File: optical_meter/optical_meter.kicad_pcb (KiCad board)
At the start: 4 copper layers, 100 x 100 mm, 47 parts, among them J1 Conn_02x04, J2 SFP+, J3 Conn_01x02_Pin, U2 LVDS -> LVTTL, U3 LVTTL -> LVDS, U5 Pico

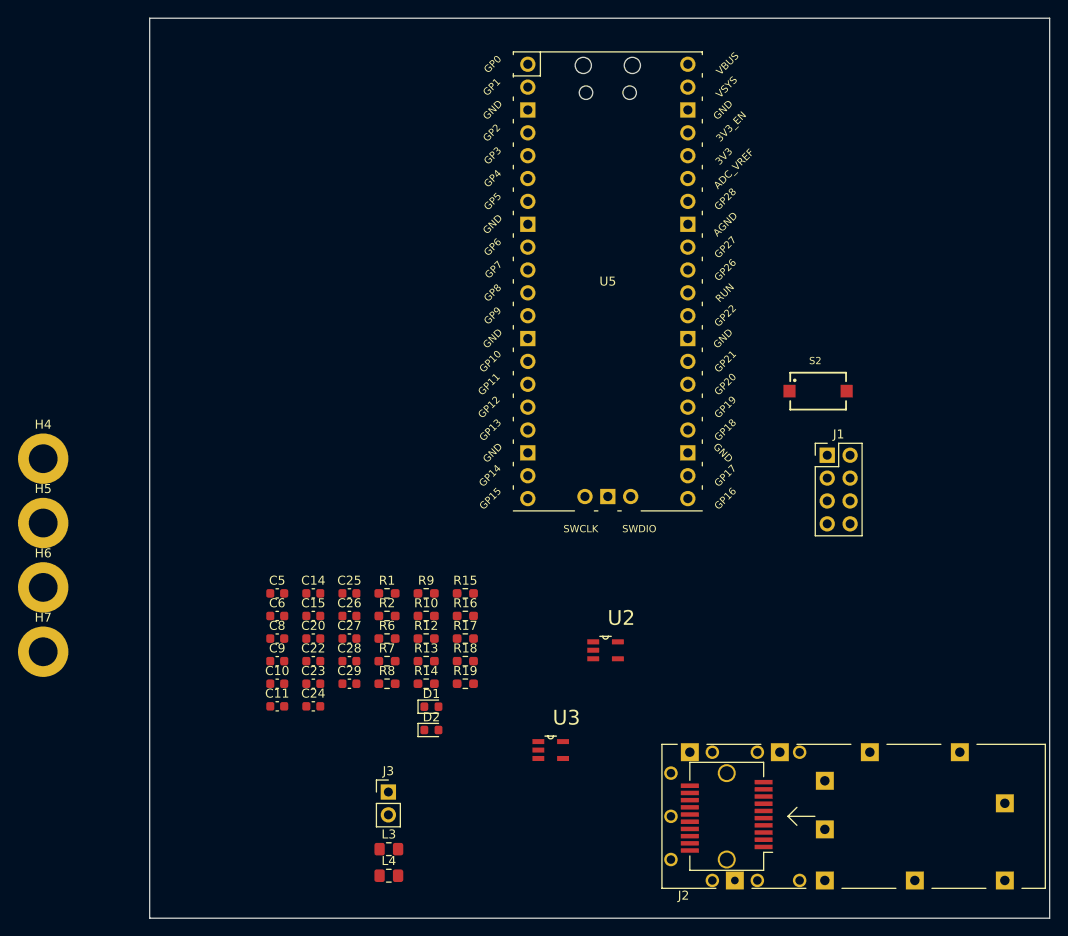
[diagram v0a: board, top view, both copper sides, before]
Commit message: Finished layout. DRC passed except for courtyard and some footprint-schematic relaitions from KiCad that do not matter
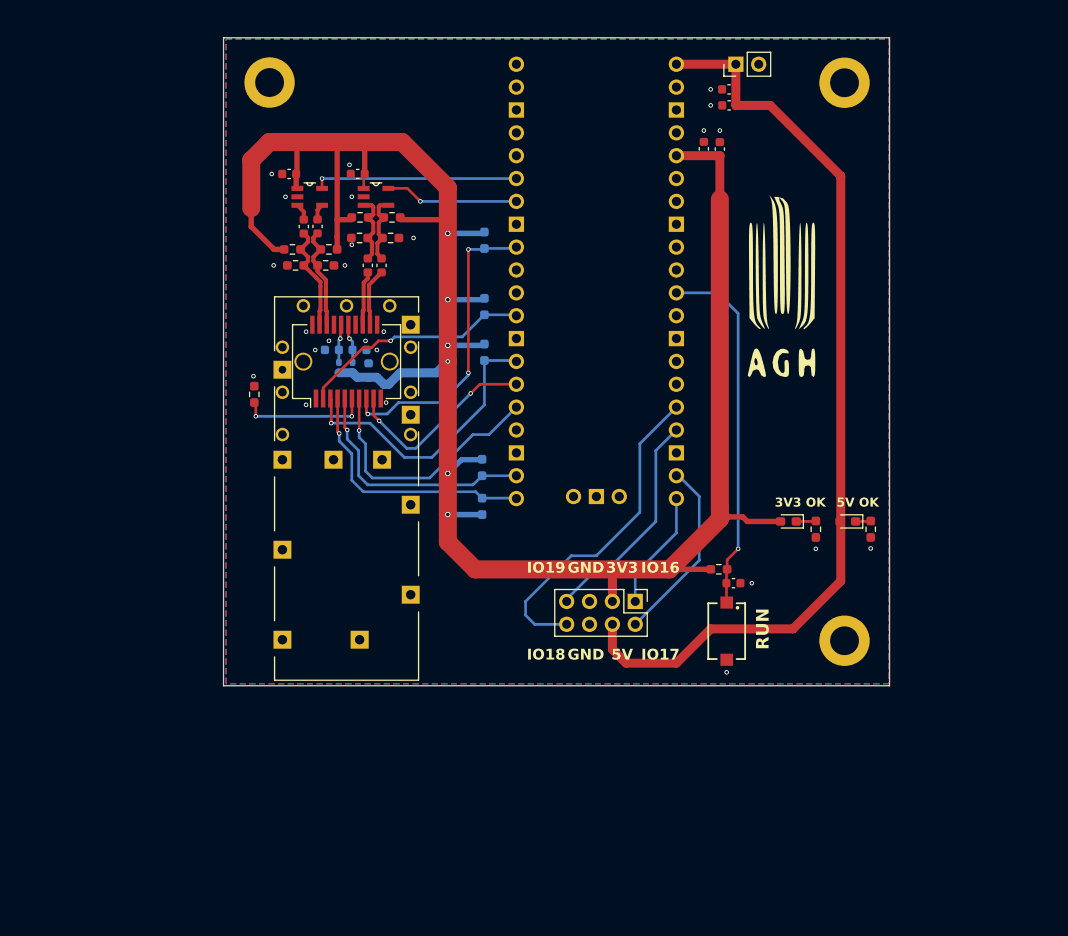
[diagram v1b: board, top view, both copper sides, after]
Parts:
- removed C11, C24, C5: 100n, Capacitor_SMD:C_0603_1608Metric
- removed C20: 2u2, Capacitor_SMD:C_0603_1608Metric
- removed H7: ~, MountingHole:MountingHole_3.2mm_M3_DIN965_Pad
- removed L3, L4: 1u, Inductor_SMD:L_0805_2012Metric_Pad1.15x1.40mm_HandSolder
- added C16: 2u2, Capacitor_SMD:C_0603_1608Metric, F.Cu at (229.9, 27.7)
- added FR1: BLM15HG102SN1D, Inductor_SMD:L_0402_1005Metric_Pad0.77x0.64mm_HandSolder, B.Cu at (186.5, 56.8)
- added FR4: BLM15HG102SN1D, Inductor_SMD:L_0402_1005Metric_Pad0.77x0.64mm_HandSolder, B.Cu at (188.0, 56.8)
- added G***: LOGO, AGH_LOGO:agh_logo, F.Cu at (235.7, 46.3)
- added R11: 4k7, Resistor_SMD:R_0603_1608Metric_Pad0.98x0.95mm_HandSolder, B.Cu at (202.4, 72.2)
- added R20: 4k7, Resistor_SMD:R_0603_1608Metric_Pad0.98x0.95mm_HandSolder, B.Cu at (202.4, 67.9)
- C10, C6, C8, R6, R7, R8: moved to B.Cu
- D1, D2: footprint Diode_SMD:D_0603_1608Metric -> LED_SMD:LED_0603_1608Metric_Pad1.05x0.95mm_HandSolder
- U2: value LVDS -> LVTTL -> FIN1002M5X
- U3: value LVTTL -> LVDS -> FIN1001M5X
- moved H5 101.6 mm to (242.7, 25.2)
- moved H4 91.3 mm to (242.7, 87.2)
- moved J3 89.6 mm to (230.6, 23.1), turned to 90 degrees
- moved C15 74.5 mm to (229.9, 25.9), turned to 180 degrees
- moved C28 69.2 mm to (227.1, 32.5), turned to 90 degrees
- moved C27 68.2 mm to (228.9, 32.5), turned to 90 degrees
- moved J2 67.2 mm to (187.4, 50.0), turned to 90 degrees
- moved U3 67.0 mm to (183.3, 37.8)
- moved H6 61.5 mm to (178.8, 25.1)
- moved U2 56.5 mm to (190.7, 37.8)
- moved R1 54.2 mm to (245.6, 74.8), turned to -90 degrees
- moved C9 54.1 mm to (181.0, 35.3)
- moved R14 52.0 mm to (192.4, 40.1)
- moved C29 51.1 mm to (182.6, 41.1), turned to -90 degrees
- moved D1 50.6 mm to (243.1, 73.9), turned to 180 degrees
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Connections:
- J1 pad 1: /GPIO17 -> /GPIO16
- J1 pad 2: /GPIO16 -> /GPIO17
- J1 pad 7: /GPIO14 -> /GPIO18
- J1 pad 8: /GPIO15 -> /GPIO19
- R16 pad 1: /U3_TD+ -> /TD+
- R17 pad 2: /U3_TD+ -> /TD+
- R18 pad 1: /U3_TD- -> /TD-
- R19 pad 2: /U3_TD- -> /TD-
- U5 pad 10: /SCL -> unconnected-(U5-GPIO7-Pad10)
- U5 pad 11: /SDA -> unconnected-(U5-GPIO8-Pad11)
- U5 pad 14: /Rpi_TX -> /TX_DISABLE
- U5 pad 19: /GPIO14 -> /SCL
- U5 pad 20: /GPIO15 -> /SDA
- U5 pad 24: unconnected-(U5-GPIO18-Pad24) -> /GPIO18
- U5 pad 25: unconnected-(U5-GPIO19-Pad25) -> /GPIO19
- U5 pad 6: /Rpi_RX -> /Rpi_TX
- U5 pad 7: /TX_DISABLE -> /Rpi_RX
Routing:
- net +3V3: track 0.00 -> 233.3 mm, vias 0 -> 6
- net +5V: track 0.00 -> 103.7 mm
- net /RUN: track 0.00 -> 40.5 mm, vias 0 -> 1
- net /GPIO19: track 0.00 -> 37.4 mm
- net /RX_LOS: track 0.00 -> 34.2 mm, vias 0 -> 3
- net /TX_DISABLE: track 0.00 -> 32.3 mm, vias 0 -> 1
- net /SDA: track 0.00 -> 28.9 mm, vias 0 -> 1
- net /RS0: track 0.00 -> 28.7 mm, vias 0 -> 1
- net /SCL: track 0.00 -> 27.6 mm, vias 0 -> 1
- net /TX_FAULT: track 0.00 -> 26.3 mm, vias 0 -> 1
- net /GPIO18: track 0.00 -> 24.8 mm
- net /Rpi_TX: track 0.00 -> 22.7 mm, vias 0 -> 1
- net /RS1: track 0.00 -> 22.2 mm, vias 0 -> 2
- net /GPIO17: track 0.00 -> 20.7 mm
- net /Rpi_RX: track 0.00 -> 14.8 mm, vias 0 -> 1
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- added copper zone on B.Cu, net GND
- added copper zone on F.Cu, net GND
- added copper zone on In1.Cu, net GND
- added copper zone on In2.Cu, net GND
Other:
- board size 100 x 100 mm -> 74 x 72 mm
- board text added: "3V3"
- board text added: "3V3 OK"
- board text added: "5V"
- board text added: "5V OK"
- board text added: "GND"
- board text added: "IO16"
- board text added: "IO17"
- board text added: "IO18"
- board text added: "IO19"
- board text added: "PCB by Filip Kulka"
- board text added: "RUN"

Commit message: changing the layout (in progress)
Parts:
- removed G***: LOGO, AGH_LOGO:agh_logo
- removed the H4 at (242.7, 87.2)
- removed H5: ~, MountingHole:MountingHole_3.2mm_M3_DIN965_Pad
- removed the H6 at (178.8, 25.1)
- added H4: ~, MountingHole:MountingHole_3.2mm_M3_DIN965_Pad, F.Cu at (226.5, 85.3)
- added H4: ~, MountingHole:MountingHole_3.2mm_M3_DIN965_Pad, F.Cu at (174.5, 85.3)
- added H6: ~, MountingHole:MountingHole_3.2mm_M3_DIN965_Pad, F.Cu at (174.5, 26.3)
- added H6: ~, MountingHole:MountingHole_3.2mm_M3_DIN965_Pad, F.Cu at (226.5, 26.3)
- C10, C27: value 2u2 -> 4u7
- R11, R20, R6, R7, R8: moved to F.Cu
- R2: value 1k -> 680R
- moved R1 39.0 mm to (226.2, 41.0), turned to 0 degrees
- moved D1 34.4 mm to (227.1, 43.5), turned to 90 degrees
- moved S2 29.1 mm to (200.6, 84.4)
- moved C25 25.7 mm to (204.7, 82.1), turned to 90 degrees
- moved R2 25.5 mm to (226.2, 53.1), turned to 0 degrees
- moved R10 22.4 mm to (206.4, 80.3), turned to -90 degrees
- moved D2 20.6 mm to (227.1, 55.6), turned to 90 degrees
- moved J3 14.4 mm to (225.4, 36.5)
- moved C27 13.0 mm to (216.2, 35.3)
- moved C28 12.8 mm to (214.6, 35.3)
- moved R17 11.4 mm to (186.5, 34.1)
- moved R19 11.4 mm to (183.1, 34.1)
- moved R18 11.2 mm to (183.1, 32.6)
- moved R16 11.1 mm to (186.5, 32.6)
- moved C29 10.9 mm to (184.1, 30.3)
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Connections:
- D1 pad 1: Net-(D1-K) -> GND
- D1 pad 2: +5V -> Net-(D1-A)
- D2 pad 1: Net-(D2-K) -> GND
- D2 pad 2: +3V3 -> Net-(D2-A)
- J1 pad 4: +5V -> +3V3
- R1 pad 1: Net-(D1-K) -> +5V
- R1 pad 2: GND -> Net-(D1-A)
- R2 pad 1: Net-(D2-K) -> +3V3
- R2 pad 2: GND -> Net-(D2-A)
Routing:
- net +3V3: track 233.3 -> 12.4 mm, vias 6 -> 15
- net +5V: track 103.7 -> 0.00 mm
- net /GPIO19: track 37.4 -> 0.00 mm
- net /RUN: track 40.5 -> 5.65 mm, vias 1 -> 0
- net /RX_LOS: track 34.2 -> 3.41 mm, vias 3 -> 0
- net /TX_DISABLE: track 32.3 -> 3.40 mm, vias 1 -> 0
- net /RS0: track 28.7 -> 0.00 mm, vias 1 -> 0
- net /SDA: track 28.9 -> 3.42 mm, vias 1 -> 0
- net /GPIO18: track 24.8 -> 0.00 mm
- net /SCL: track 27.6 -> 3.40 mm, vias 1 -> 0
- net /TX_FAULT: track 26.3 -> 3.40 mm, vias 1 -> 0
- net /RS1: track 22.2 -> 0.00 mm, vias 2 -> 0
- net /GPIO17: track 20.7 -> 0.00 mm
- net Net-(J2-MOD_ABS): track 14.2 -> 0.00 mm, vias 2 -> 0
- net /GPIO16: track 13.3 -> 0.00 mm
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- added copper zone on F.Cu, net +3V3
- added copper zone on In2.Cu, net +3V3
- added copper zone on In2.Cu, net +5V
- removed copper zone on B.Cu, net GND
- removed copper zone on F.Cu, net GND
- removed copper zone on In2.Cu, net GND
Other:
- board size 74 x 72 mm -> 60 x 67 mm
- board text added: "+3V3"
- board text added: "+5V"
- board text added: "Optical Power Analyzer"
- board text removed: "3V3"
- board text removed: "3V3 OK"
- board text removed: "5V"
- board text removed: "5V OK"
- board text removed: "GND"
- board text removed: "IO16"
- board text removed: "IO17"
- board text removed: "IO18"
- board text removed: "IO19"
- board text removed: "PCB by Filip Kulka"
- board text removed: "RUN"
